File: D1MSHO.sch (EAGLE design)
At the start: 2 parts

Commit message: Added license and preview images, and updated README
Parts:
- renumbered JP3 to H1, JP4 to H2
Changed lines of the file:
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@@
 </classes>
 <parts>
-<part name="JP3" library="freetronics-original" deviceset="M08" device=""/>
-<part name="JP4" library="freetronics-original" deviceset="M08" device=""/>
+<part name="H1" library="freetronics-original" deviceset="M08" device=""/>
+<part name="H2" library="freetronics-original" deviceset="M08" device=""/>
 <part name="U$1" library="freetronics-original" deviceset="5V" device=""/>
 <part name="P+1" library="freetronics-original" deviceset="3.3V" device=""/>
@@
 </plain>
 <instances>
-<instance part="JP3" gate="G$1" x="26.67" y="104.14" rot="MR180"/>
-<instance part="JP4" gate="G$1" x="223.52" y="104.14" rot="R180"/>
+<instance part="H1" gate="G$1" x="26.67" y="104.14" rot="MR180"/>
+<instance part="H2" gate="G$1" x="223.52" y="104.14" rot="R180"/>
 <instance part="U$1" gate="G$1" x="205.74" y="116.84"/>
 <instance part="P+1" gate="G$1" x="45.72" y="116.84"/>
@@
 <net name="GND" class="0">
 <segment>
-<pinref part="JP4" gate="G$1" pin="7"/>
+<pinref part="H2" gate="G$1" pin="7"/>
 <wire x1="218.44" y1="96.52" x2="208.28" y2="96.52" width="0.1524" layer="91"/>
 <label x="212.09" y="96.52" size="1.778" layer="95"/>
@@
 <net name="D1" class="0">
 <segment>
-<pinref part="JP4" gate="G$1" pin="3"/>
+<pinref part="H2" gate="G$1" pin="3"/>
 <wire x1="218.44" y1="106.68" x2="210.82" y2="106.68" width="0.1524" layer="91"/>
 <label x="212.09" y="106.68" size="1.778" layer="95"/>
@@
 <segment>
 <wire x1="218.44" y1="104.14" x2="210.82" y2="104.14" width="0.1524" layer="91"/>
-<pinref part="JP4" gate="G$1" pin="4"/>
+<pinref part="H2" gate="G$1" pin="4"/>
 <label x="212.09" y="104.14" size="1.778" layer="95"/>
 </segment>
@@
 <net name="D5" class="0">
 <segment>
-<pinref part="JP3" gate="G$1" pin="4"/>
+<pinref part="H1" gate="G$1" pin="4"/>
 <wire x1="31.75" y1="104.14" x2="40.64" y2="104.14" width="0.1524" layer="91"/>
 <label x="33.02" y="104.14" size="1.778" layer="95"/>
@@
 <wire x1="31.75" y1="101.6" x2="40.64" y2="101.6" width="0.1524" layer="91"/>
 <label x="33.02" y="101.6" size="1.778" layer="95"/>
-<pinref part="JP3" gate="G$1" pin="5"/>
+<pinref part="H1" gate="G$1" pin="5"/>
 </segment>
 </net>
 <net name="D7" class="0">
 <segment>
-<pinref part="JP3" gate="G$1" pin="6"/>
+<pinref part="H1" gate="G$1" pin="6"/>
 <wire x1="31.75" y1="99.06" x2="40.64" y2="99.06" width="0.1524" layer="91"/>
 <label x="33.02" y="99.06" size="1.778" layer="95"/>
@@
 <net name="D8" class="0">
 <segment>
-<pinref part="JP3" gate="G$1" pin="7"/>
+<pinref part="H1" gate="G$1" pin="7"/>
 <wire x1="31.75" y1="96.52" x2="40.64" y2="96.52" width="0.1524" layer="91"/>
 <label x="33.02" y="96.52" size="1.778" layer="95"/>
@@
 <net name="A0" class="0">
 <segment>
-<pinref part="JP3" gate="G$1" pin="2"/>
+<pinref part="H1" gate="G$1" pin="2"/>
 <wire x1="31.75" y1="109.22" x2="40.64" y2="109.22" width="0.1524" layer="91"/>
 <label x="33.02" y="109.22" size="1.778" layer="95"/>
@@
 <label x="33.02" y="111.76" size="1.778" layer="95"/>
 <wire x1="31.75" y1="111.76" x2="40.64" y2="111.76" width="0.1524" layer="91"/>
-<pinref part="JP3" gate="G$1" pin="1"/>
+<pinref part="H1" gate="G$1" pin="1"/>
 </segment>
 </net>
 <net name="D0" class="0">
 <segment>
-<pinref part="JP3" gate="G$1" pin="3"/>
+<pinref part="H1" gate="G$1" pin="3"/>
 <wire x1="31.75" y1="106.68" x2="40.64" y2="106.68" width="0.1524" layer="91"/>
 <label x="33.02" y="106.68" size="1.778" layer="95"/>
@@
 <wire x1="218.44" y1="111.76" x2="210.82" y2="111.76" width="0.1524" layer="91"/>
 <label x="212.09" y="111.76" size="1.778" layer="95"/>
-<pinref part="JP4" gate="G$1" pin="1"/>
+<pinref part="H2" gate="G$1" pin="1"/>
 </segment>
 </net>
 <net name="RX" class="0">
 <segment>
-<pinref part="JP4" gate="G$1" pin="2"/>
+<pinref part="H2" gate="G$1" pin="2"/>
 <wire x1="218.44" y1="109.22" x2="210.82" y2="109.22" width="0.1524" layer="91"/>
 <label x="212.09" y="109.22" size="1.778" layer="95"/>
@@
 <net name="D4" class="0">
 <segment>
-<pinref part="JP4" gate="G$1" pin="6"/>
+<pinref part="H2" gate="G$1" pin="6"/>
 <wire x1="218.44" y1="99.06" x2="210.82" y2="99.06" width="0.1524" layer="91"/>
 <label x="212.09" y="99.06" size="1.778" layer="95"/>
@@
 <net name="D3" class="0">
 <segment>
-<pinref part="JP4" gate="G$1" pin="5"/>
+<pinref part="H2" gate="G$1" pin="5"/>
 <wire x1="218.44" y1="101.6" x2="210.82" y2="101.6" width="0.1524" layer="91"/>
 <label x="212.09" y="101.6" size="1.778" layer="95"/>
@@
 <net name="5V" class="0">
 <segment>
-<pinref part="JP4" gate="G$1" pin="8"/>
+<pinref part="H2" gate="G$1" pin="8"/>
 <label x="212.09" y="93.98" size="1.778" layer="95"/>
 <wire x1="218.44" y1="93.98" x2="205.74" y2="93.98" width="0.1524" layer="91"/>
@@
 <net name="3.3V" class="0">
 <segment>
-<pinref part="JP3" gate="G$1" pin="8"/>
+<pinref part="H1" gate="G$1" pin="8"/>
 <wire x1="31.75" y1="93.98" x2="45.72" y2="93.98" width="0.1524" layer="91"/>
 <label x="33.02" y="93.98" size="1.778" layer="95"/>

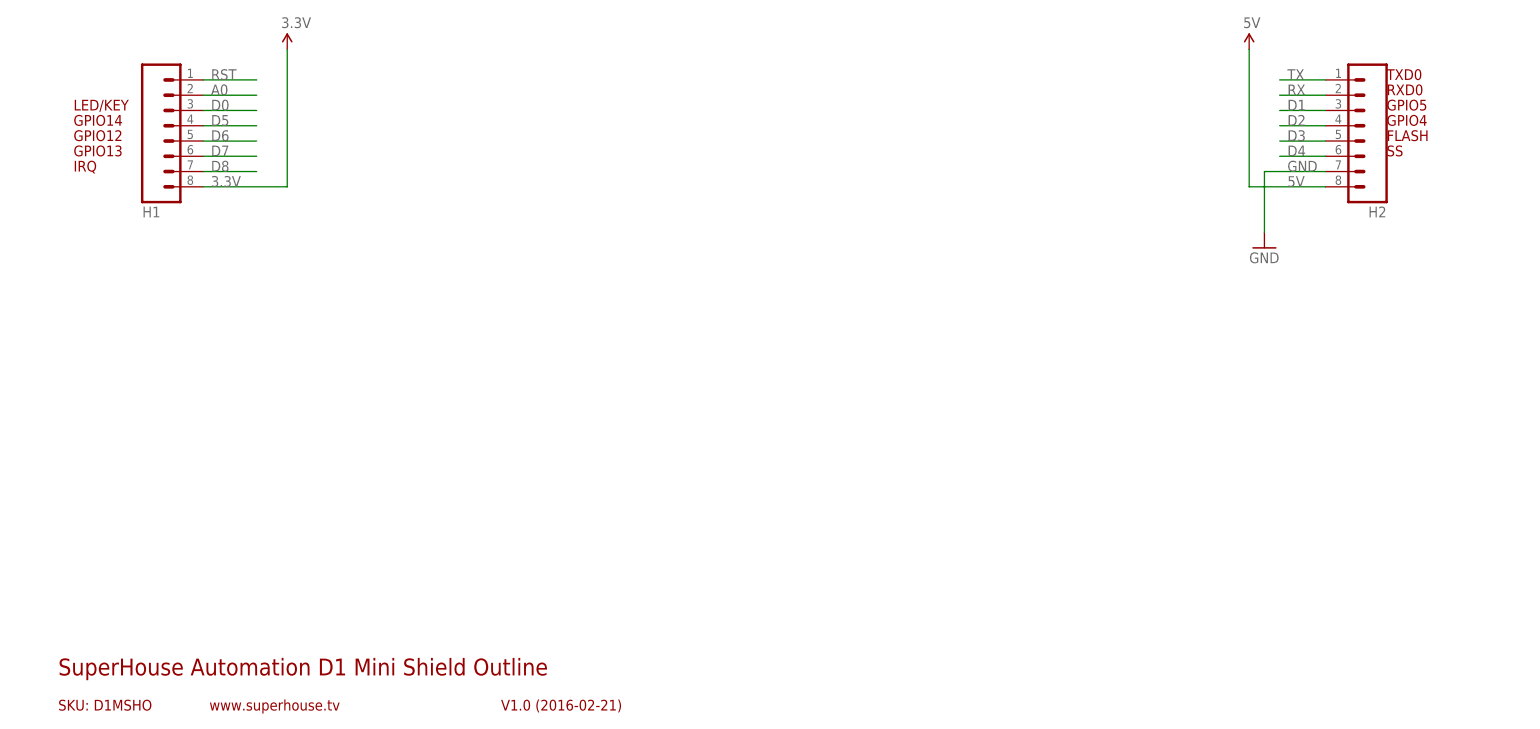
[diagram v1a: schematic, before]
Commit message: Added pin information to schematic
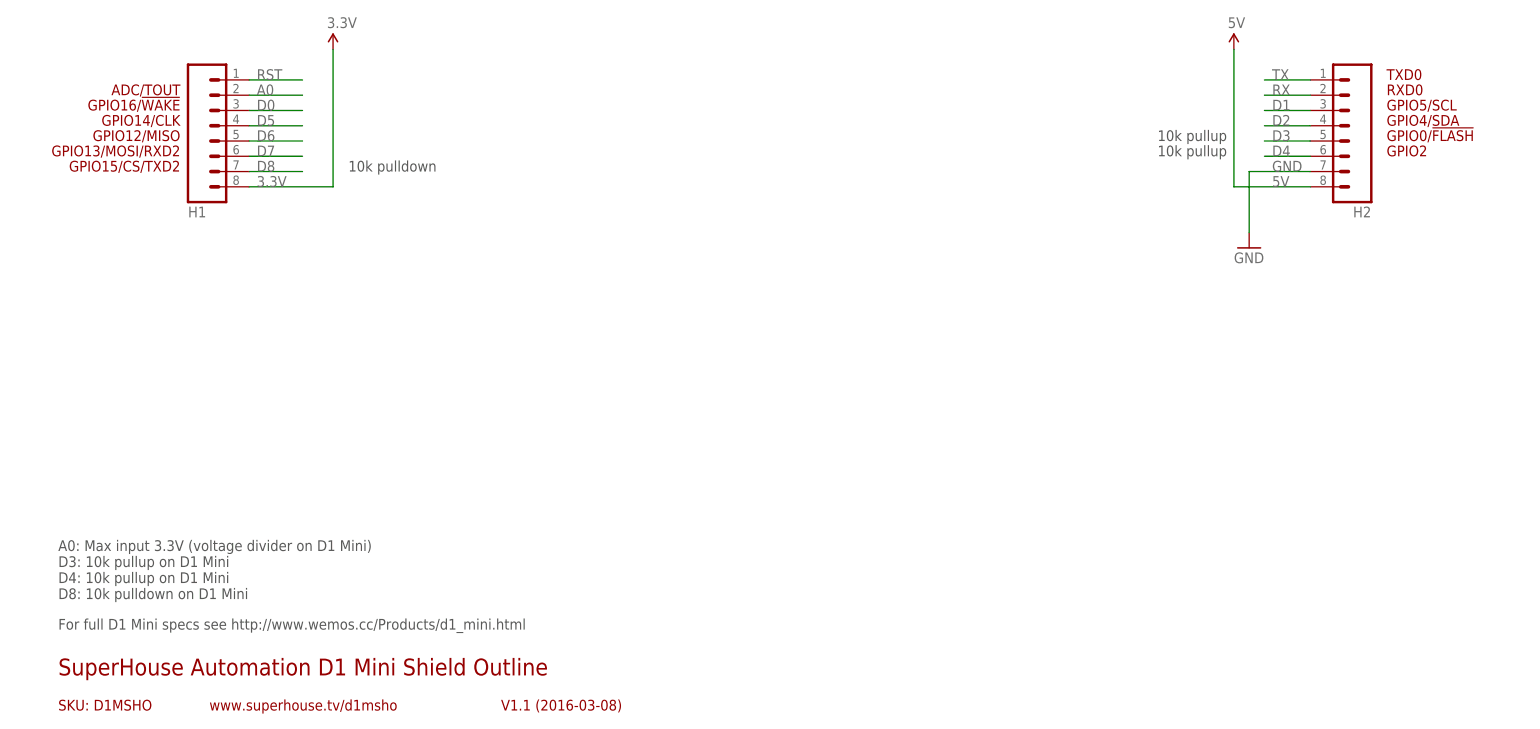
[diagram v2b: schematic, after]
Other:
- note added: "10k pulldown"
- note added: "10k pullup"
- note added: "A0: Max input 3.3V (voltage divider on D1 Mini) D3: 10k pullup on D1 Mini D4: 10k pullup on D1 Mini D8: 10k pulldown on D1 Mini"
- note added: "ADC/TOUT"
- note added: "For full D1 Mini specs see http://www.wemos.cc/Products/d1_mini.html"
- note added: "GPIO0/!FLASH"
- note added: "GPIO12/MISO"
- note added: "GPIO13/MOSI/RXD2"
- note added: "GPIO14/CLK"
- note added: "GPIO15/CS/TXD2"
- note added: "GPIO16/!WAKE"
- note added: "GPIO2"
- note added: "GPIO4/SDA"
- note added: "GPIO5/SCL"
- note added: "V1.1 (2016-03-08)"
- note added: "www.superhouse.tv/d1msho"
- note removed: "FLASH"
- note removed: "GPIO12"
- note removed: "GPIO13"
- note removed: "GPIO14"
- note removed: "GPIO4"
- note removed: "GPIO5"
- note removed: "IRQ"
- note removed: "LED/KEY"
- note removed: "SS"
- note removed: "V1.0 (2016-02-21)"
- note removed: "www.superhouse.tv"
- moved on the sheet: H1, H2
